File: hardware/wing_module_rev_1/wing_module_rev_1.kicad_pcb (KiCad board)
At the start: 4 copper layers, 50 x 21 mm, 64 parts, among them J1 Conn_01x03, J2 Conn_01x03, J3 Conn_ST_STDC14, J4 Conn_01x04, J5 STRAIN, J6 TORSION, J7 Conn_01x04, J8 Conn_01x04, U1 STM32F103T8U6, U2 TPS563201, U3 BL9161G-33, U4 TPS7A8101, U5 ADS131M03IRUK, U6 TCAN3403

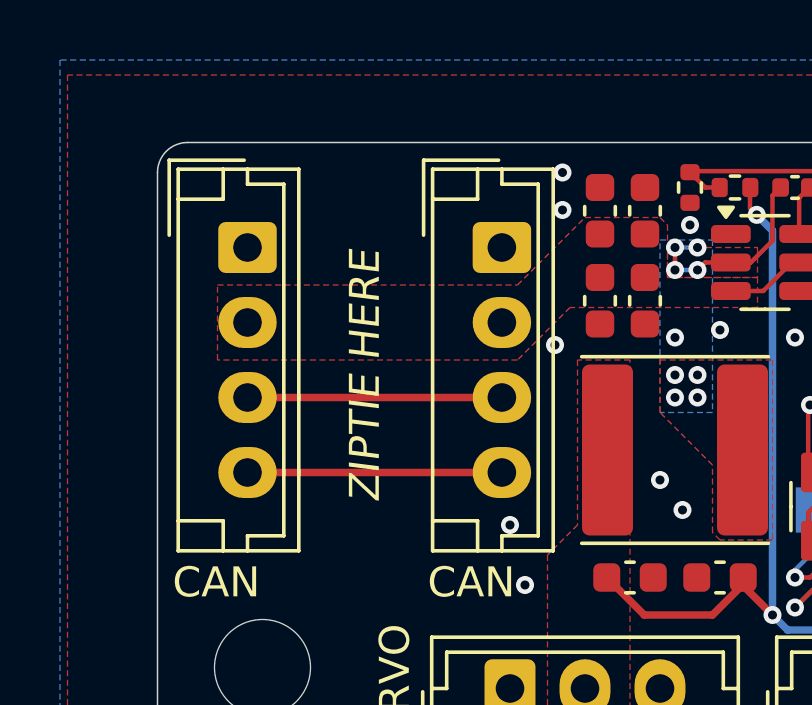
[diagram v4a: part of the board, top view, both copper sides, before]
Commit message: Added JLC tracking marker
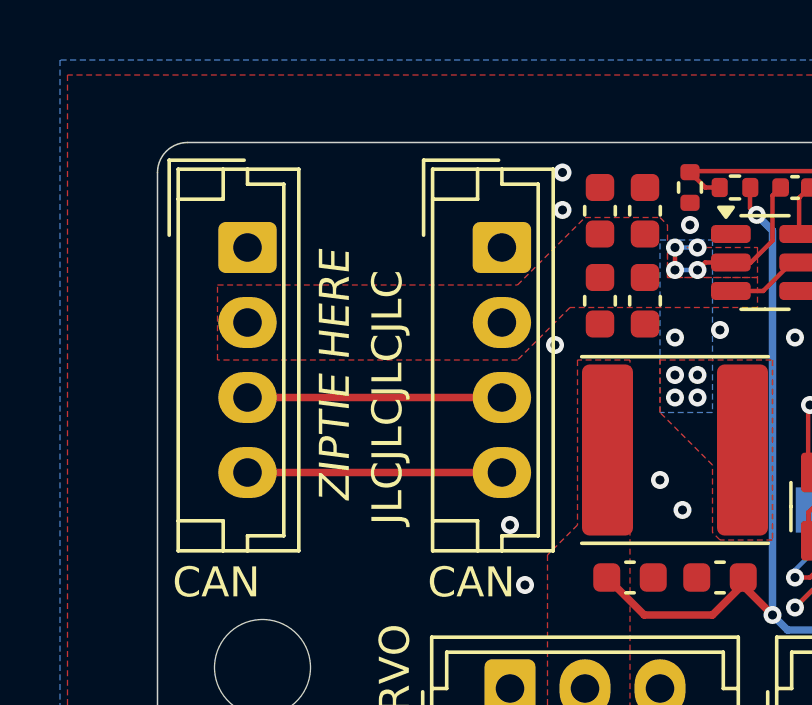
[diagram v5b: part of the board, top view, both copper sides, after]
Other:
- board text added: "JLCJLCJLCJLC"
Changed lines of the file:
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@@
 	)
 	(gr_text "ZIPTIE HERE"
-		(at 131 93 90)
+		(at 130 93 90)
 		(layer "F.SilkS")
 		(effects
 			(font
 				(size 1 1)
-				(thickness 0.1)
+				(thickness 0.125)
 				(italic yes)
 			)
@@
 		(effects
 			(font
+				(size 1 1)
+				(thickness 0.125)
+			)
+			(justify left bottom)
+		)
+	)
+	(gr_text "JLCJLCJLCJLC"
+		(at 131.75 93.75 90)
+		(layer "F.SilkS")
+		(effects
+			(font
